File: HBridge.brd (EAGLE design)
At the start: 59.7 x 53.3 mm, 42 parts, among them IC1 74HC08D, IC2 A4954, J1 In 3/4, J2 Power, J3 In 1/2, J4 Output A, J5 Output B, J6 Digital_8_13, J7 Analog, J8 Digital_0_7

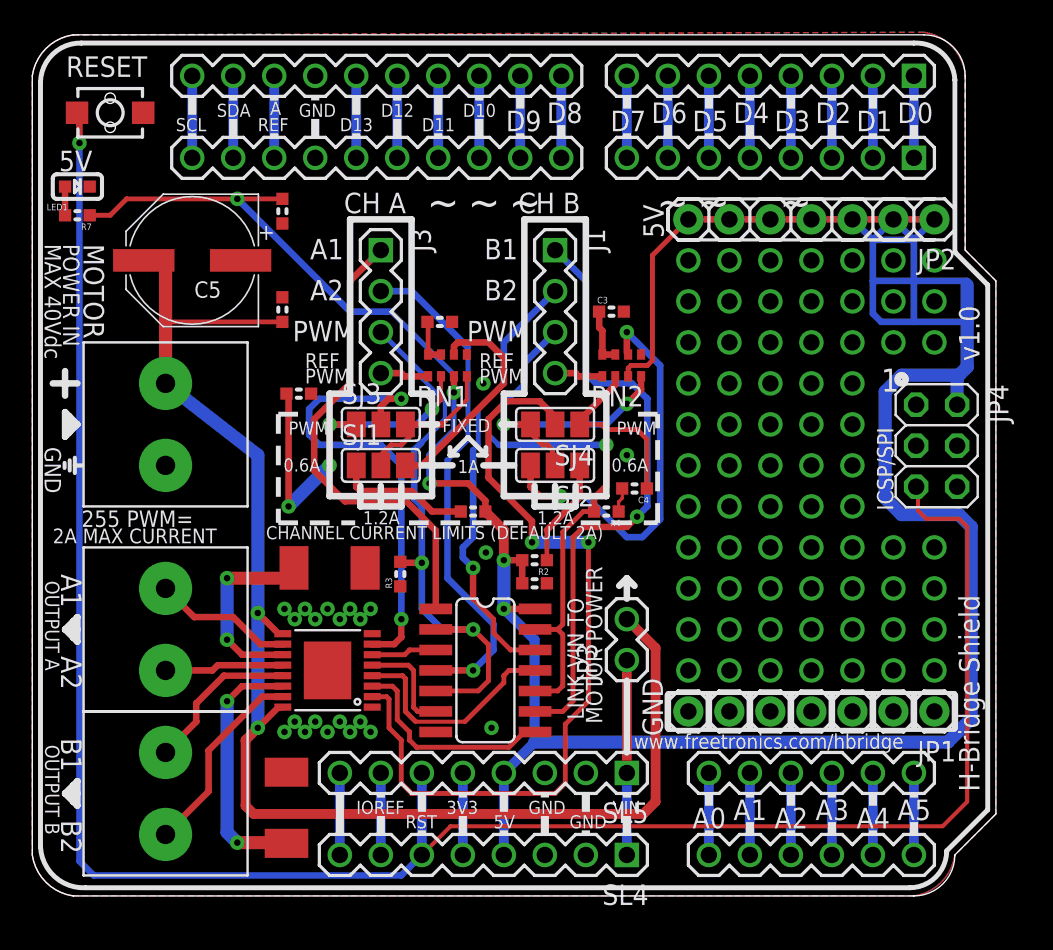
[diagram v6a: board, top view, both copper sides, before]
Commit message: Made track widths consistent; renamed parts; relocated designators, improved silkscreen
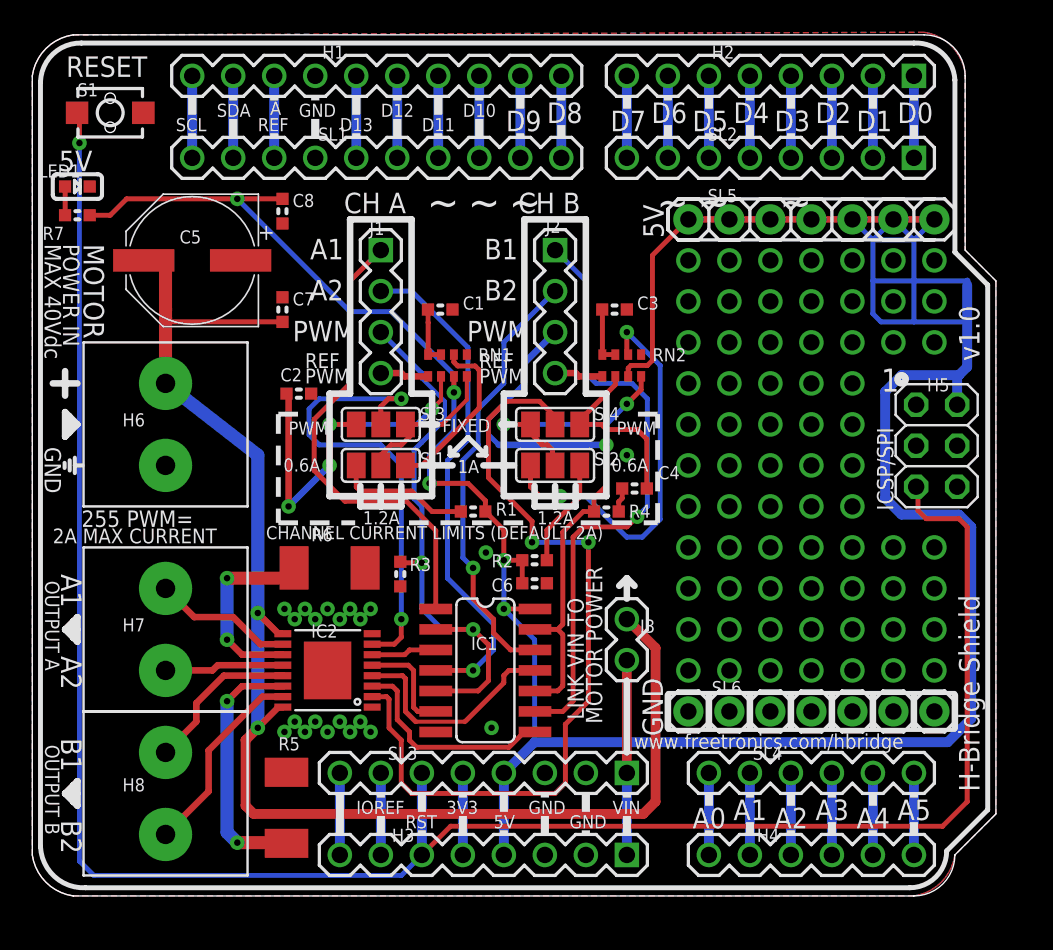
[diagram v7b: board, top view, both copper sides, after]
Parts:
- removed JP2: +5V, SparkFun:1X07
- removed JP3: (no value), freetronics-master-v1:1X02
- added H3: Power, freetronics:1X08
- added H6: Power, con-wago-508:W237-132
- C5: value 100 uF -> 100uF
- C6: value 100 nF -> 100nF
- C7: value 220 nF -> 220nF
- H5: value (none) -> ICSP
- J1: value In 3/4 -> In 1/2
- J2: value Power -> In 3/4; device con-wago-508:W237-132 -> freetronics-master-v1:1X04
- J3: value In 1/2 -> (none); device freetronics-master-v1:1X04 -> freetronics-master-v1:1X02
- R3, R4: value 10k -> 10K
- SL2: value Analog -> Digital_0_7; device freetronics:1X06 -> freetronics:1X08
- SL3: value Digital_0_7 -> Power
- SL4: value Digital_0_7 -> Analog; device freetronics:1X08 -> freetronics:1X06
- SL5: value Digital_0_7 -> +5V; device freetronics:1X08 -> SparkFun:1X07
- moved SL3 42.0 mm to (36.8, 7.62)
- moved SL2 40.2 mm to (54.6, 45.7), turned to 180 degrees
- moved SL5 39.2 mm to (55.9, 41.9)
- moved J3 29.6 mm to (36.8, 14.6), turned to 90 degrees
- moved J2 25.9 mm to (32.4, 40.0)
- moved J1 10.8 mm to (21.6, 40.0)
- moved SL4 7.18 mm to (41.9, 7.62), turned to 0 degrees
- moved C1 0.76 mm to (25.3, 36.3)
- moved C3 0.23 mm to (36.1, 36.3)
- renumbered J4 to H7, J5 to H8, J6 to H1, J7 to H4, J8 to H2, JP1 to SL6, JP4 to H5
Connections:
- net +5V: now also H3.4, SL3.4, SL5.1, SL5.2, SL5.3, SL5.5, SL5.6, SL5.7; no longer JP2.1, JP2.2, JP2.3, JP2.4, JP2.5, JP2.6, JP2.7, SL4.4
- net 3V3: now also H3.5, SL3.5; no longer SL4.5, SL5.5
- net A0: now also SL4.1; no longer SL2.1
- net A1: now also SL4.2; no longer SL2.2
- net A2: now also SL4.3; no longer SL2.3
- net A3: now also SL4.4; no longer SL2.4
- net A4: now also SL4.5; no longer SL2.5
- net A5: now also SL4.6; no longer SL2.6
- net D0_RX: now also SL2.1; no longer SL3.1
- net D1_TX: now also SL2.2; no longer SL3.2
- net D2: now also SL2.3; no longer SL3.3
- net D3: now also SL2.4; no longer SL3.4
- net D4: now also SL2.5; no longer SL3.5
- net D5: now also SL2.6; no longer SL3.6
- net D6: now also SL2.7; no longer SL3.7
- net D7: now also SL2.8; no longer SL3.8
- net GND: now also H3.2, H3.3, H6.2, SL3.2, SL3.3; no longer J2.2, SL4.2, SL4.3, SL5.2, SL5.3
- net IN1: now also J1.1; no longer J3.1
- net IN2: now also J1.2; no longer J3.2
- net IN3: now also J2.1; no longer J1.1
- net IN4: now also J2.2; no longer J1.2
- net IOREF: now also H3.7, SL3.7; no longer SL4.7, SL5.7
- net PWM12: now also J1.3; no longer J3.3
- net PWM34: now also J2.3; no longer J1.3
- net REF_PWM_12: now also J1.4; no longer J3.4
- net REF_PWM_34: now also J2.4; no longer J1.4
- net RESET: now also H3.6, SL3.6; no longer SL4.6, SL5.6
- net UNUSED: now also H3.8, SL3.8; no longer SL4.8, SL5.8
- net VBB: now also H6.1, J3.2; no longer J2.1, JP3.2
- net VIN: now also H3.1, J3.1, SL3.1; no longer JP3.1, SL4.1, SL5.1
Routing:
- net N$15: track 13.9 -> 10.6 mm
- net N$19: track 2.84 -> 3.59 mm
- net GND: vias 22 -> 21
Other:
- board text added: "(c) 2012 Freetronics Pty Ltd"
- board text added: "S1"
- board text removed: "(c) 2012 Freetronics"
